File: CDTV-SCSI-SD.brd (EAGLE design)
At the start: 77.6 x 107.3 mm, 25 parts, among them CN1 CDTV-EXPANSION, IC1 74HC245N, IC2 WD33C93A, X1 057-050-1

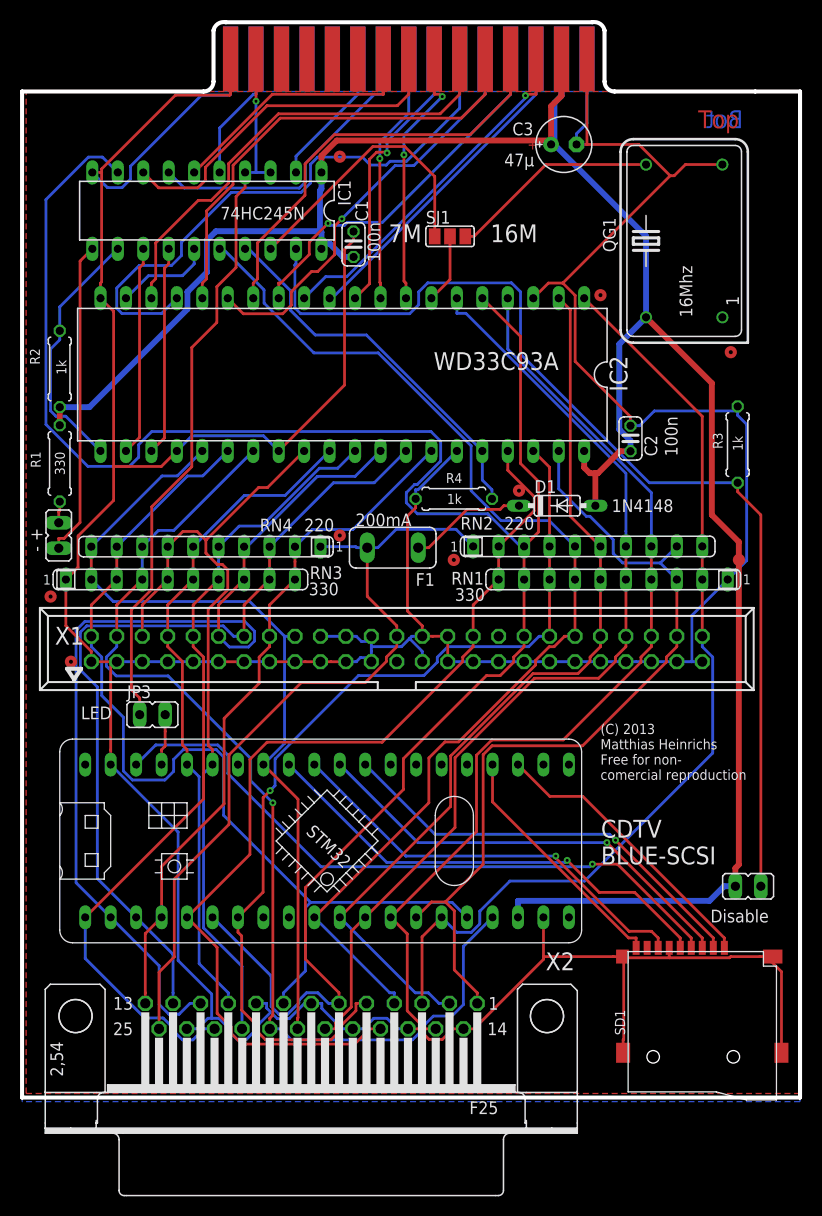
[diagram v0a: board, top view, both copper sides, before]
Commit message: (fix), db25 was male instead of female
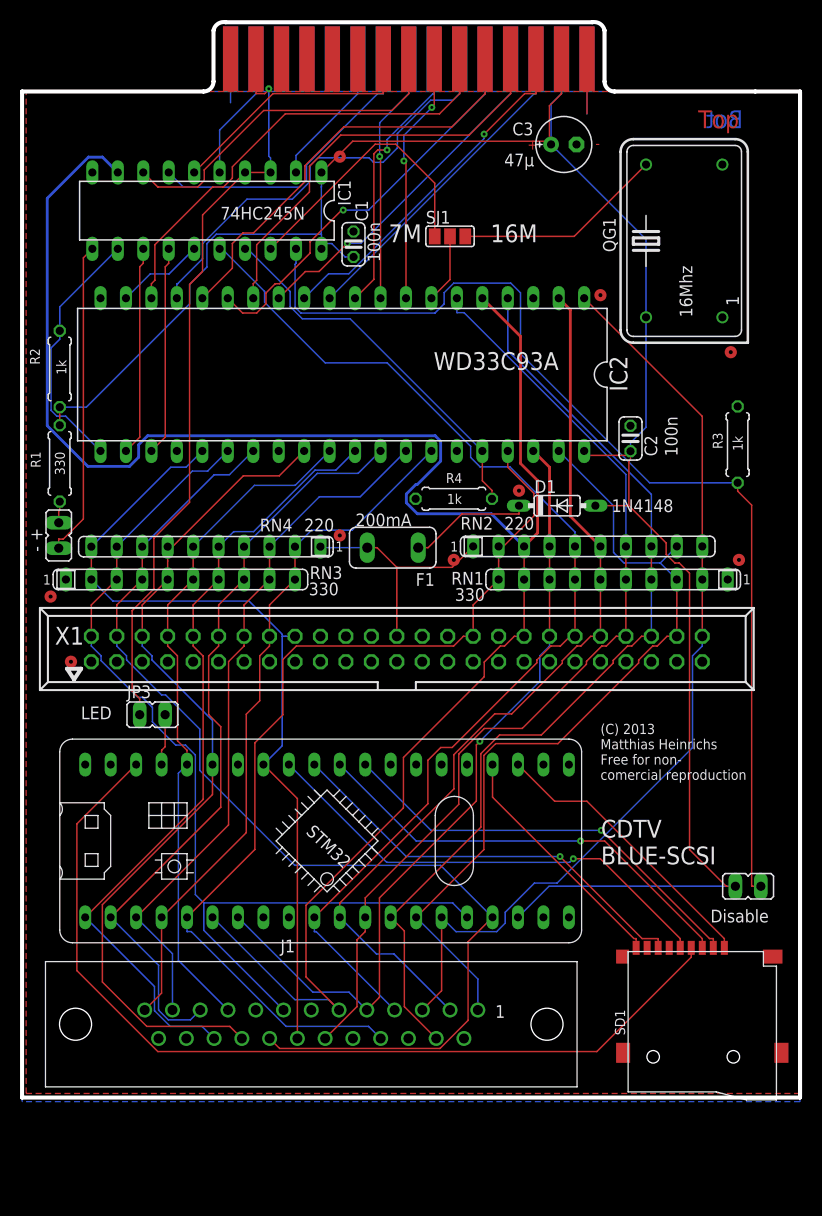
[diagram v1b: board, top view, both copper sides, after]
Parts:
- removed X2: (no value), SparkFun:F25H
- added J1: (no value), InputOutputIO (rev18a):61802529321
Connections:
- new net TERM: J1.25
- net /ACK: now also J1.5; no longer X2.5
- net /ATN: now also J1.17; no longer X2.17
- net /BSY: now also J1.6; no longer X2.6
- net /MSG: now also J1.2; no longer X2.2
- net /REQ: now also J1.1; no longer X2.1
- net /SCSI_RST: now also J1.4; no longer X2.4
- net /SEL: now also J1.19; no longer X2.19
- net CD: now also J1.15; no longer X2.15
- net DB0: now also J1.8; no longer X2.8
- net DB1: now also J1.21; no longer X2.21
- net DB2: now also J1.22; no longer X2.22
- net DB3: now also J1.10; no longer X2.10
- net DB4: now also J1.23; no longer X2.23
- net DB5: now also J1.11; no longer X2.11
- net DB6: now also J1.12; no longer X2.12
- net DB7: now also J1.13; no longer X2.13
- net DBP: now also J1.20; no longer X2.20
- net GND: now also J1.14, J1.16, J1.18, J1.24, J1.7, J1.9; no longer X2.14, X2.16, X2.18, X2.24, X2.7, X2.9
- net IO: now also J1.3; no longer X2.3
- net TERM_P: no longer X2.25
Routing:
- net GND: track 479.1 -> 18.6 mm
- net TERM_P: track 79.5 -> 23.8 mm
- net +3V3: track 66.5 -> 92.5 mm, vias 1 -> 0
- net DB5: track 97.1 -> 77.3 mm
- net VCC: track 224.1 -> 206.0 mm
- net DB6: track 85.4 -> 70.8 mm
- net /ACK: track 94.8 -> 80.7 mm
- net SD6: track 58.0 -> 44.0 mm
- net DB2: track 81.2 -> 86.0 mm
- net DB1: track 106.0 -> 110.0 mm, vias 1 -> 0
- net SD5: track 46.1 -> 42.5 mm
- net /BSY: track 201.4 -> 197.9 mm
- net /IFRST: track 73.0 -> 75.0 mm
- net IO: track 95.9 -> 94.0 mm
- net SD2: track 36.9 -> 35.1 mm
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
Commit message: (fix), MOSI and SCK were switched
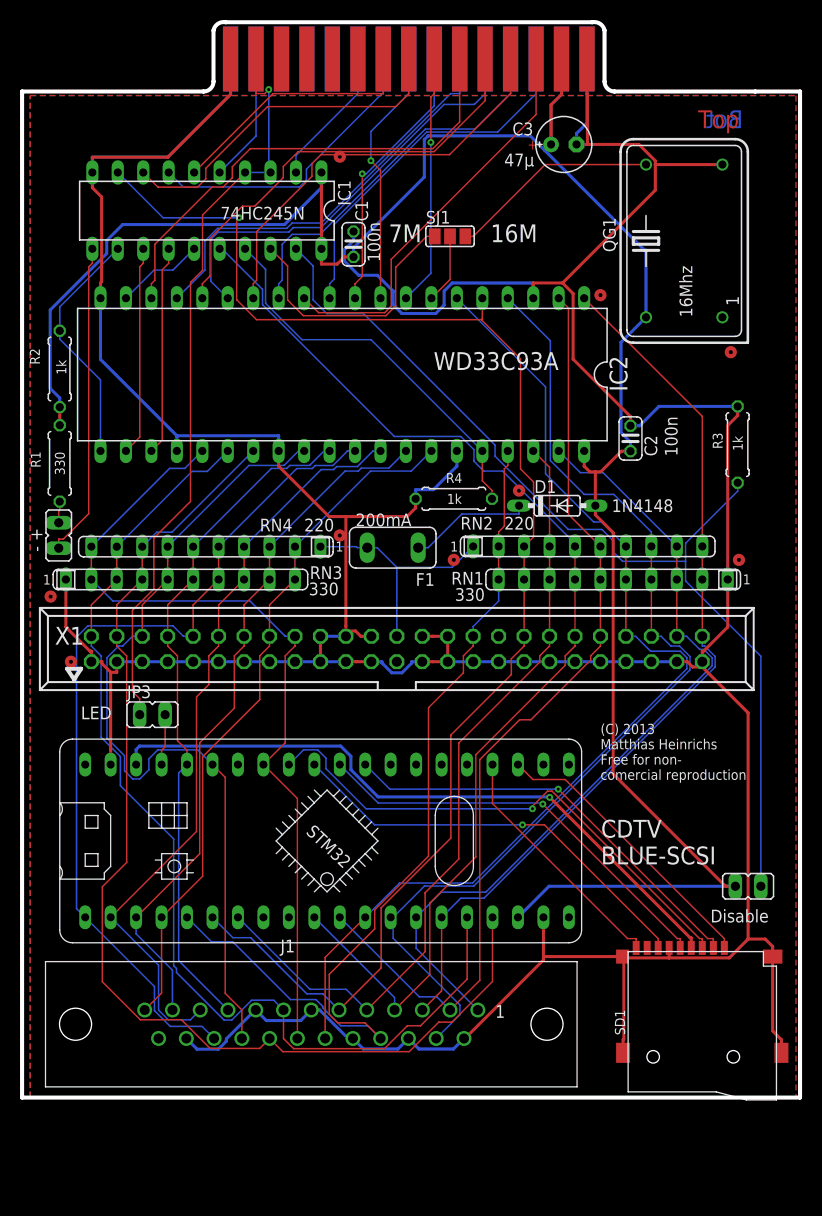
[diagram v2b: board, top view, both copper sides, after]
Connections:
- net MOSI: now also U$1.P$29; no longer U$1.P$31
- net SCK: now also U$1.P$31; no longer U$1.P$29
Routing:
- net GND: track 18.6 -> 480.9 mm
- net /BSY: track 197.9 -> 145.2 mm, vias 0 -> 1
- net +3V3: track 92.5 -> 66.7 mm, vias 0 -> 1
- net VCC: track 206.0 -> 218.7 mm
- net DB0: track 98.0 -> 106.6 mm
- net /SEL: track 96.8 -> 105.3 mm
- net MOSI: track 44.3 -> 52.8 mm
- net CD: track 95.7 -> 103.3 mm
- net DB4: track 80.2 -> 87.7 mm
- net SCK: track 47.5 -> 42.1 mm
- net /ENABLE: track 105.7 -> 100.6 mm
- net SD1: track 35.3 -> 40.2 mm, vias 1 -> 0
- net SD0: track 32.5 -> 36.6 mm
- net IO: track 94.0 -> 90.0 mm
- net /SCSI_RST: track 112.1 -> 115.8 mm
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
